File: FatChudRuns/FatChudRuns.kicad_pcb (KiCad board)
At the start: 4 copper layers, 96.9 x 73.9 mm, 104 parts, among them J1 RJ45_Pulse_JXD6-0001NL, J2 Z-21320110021001, J3 FTSH-107-01-L-DV-K-P, J4 TYPE-C-31-M-12, SW1 TS-1187A-B-A-B, SW5 1825360-3, U1 STM32F107RBT6, U2 DP83848I, U3 USBLC6-2SC6, U4 ST730M33R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

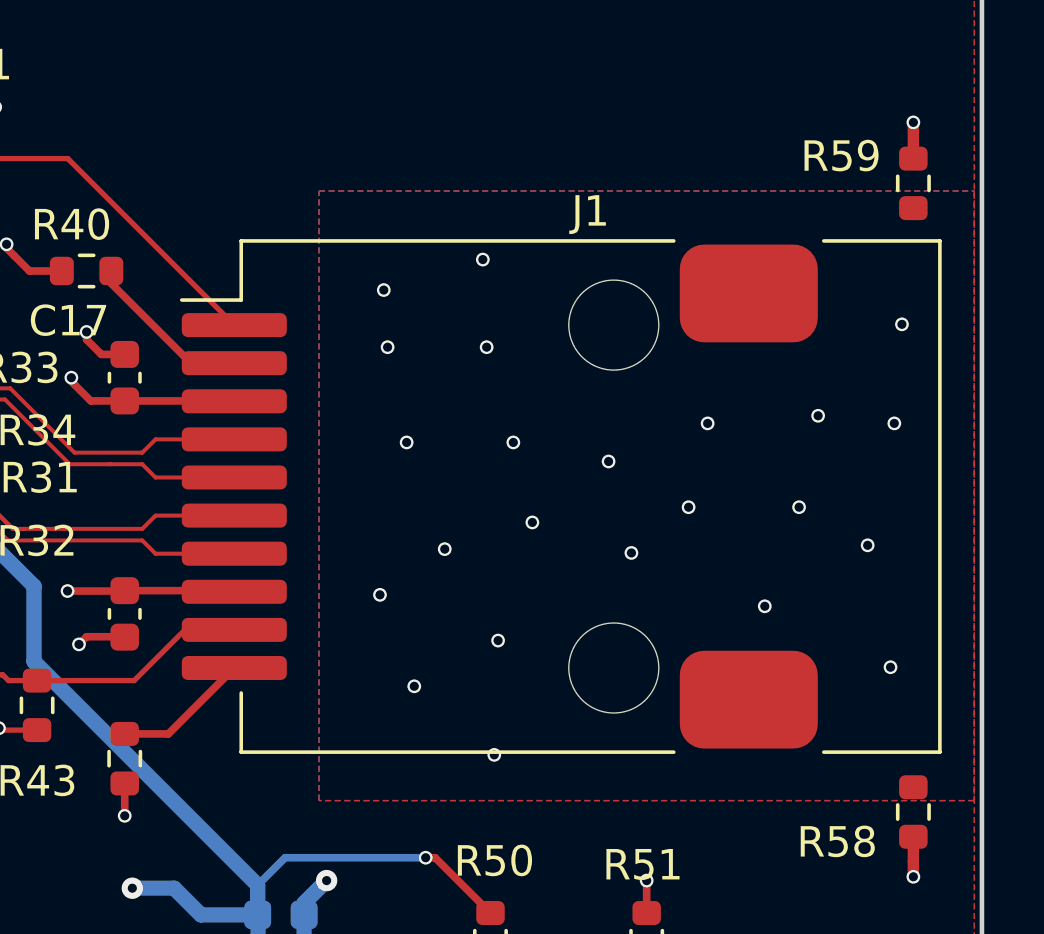
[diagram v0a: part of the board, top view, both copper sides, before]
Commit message: updated 3d model footprint for Rj45 (created new library)
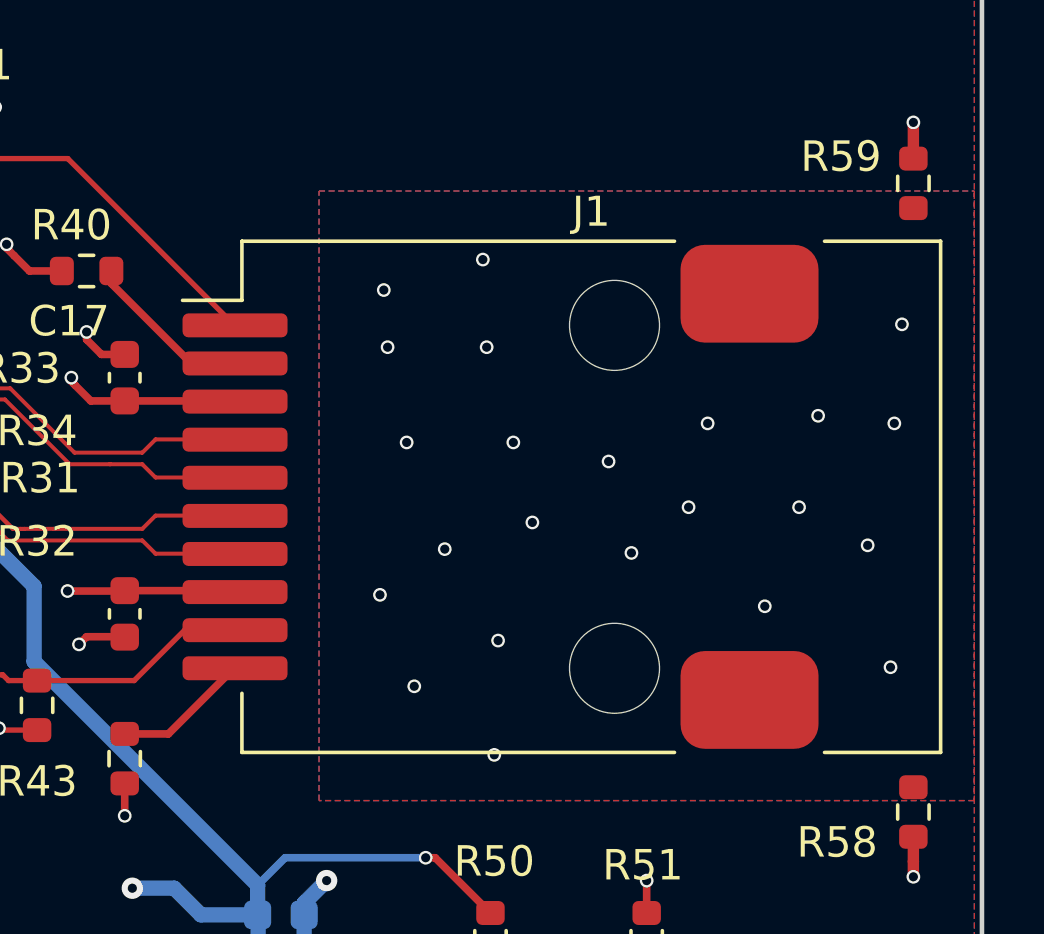
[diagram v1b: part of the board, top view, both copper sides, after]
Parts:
- J1: footprint Connector_RJ:RJ45_Pulse_JXD6-0001NL_Horizontal -> JXD6-0001NL:RJ45_Pulse_JXD6-0001NL_Horizontal

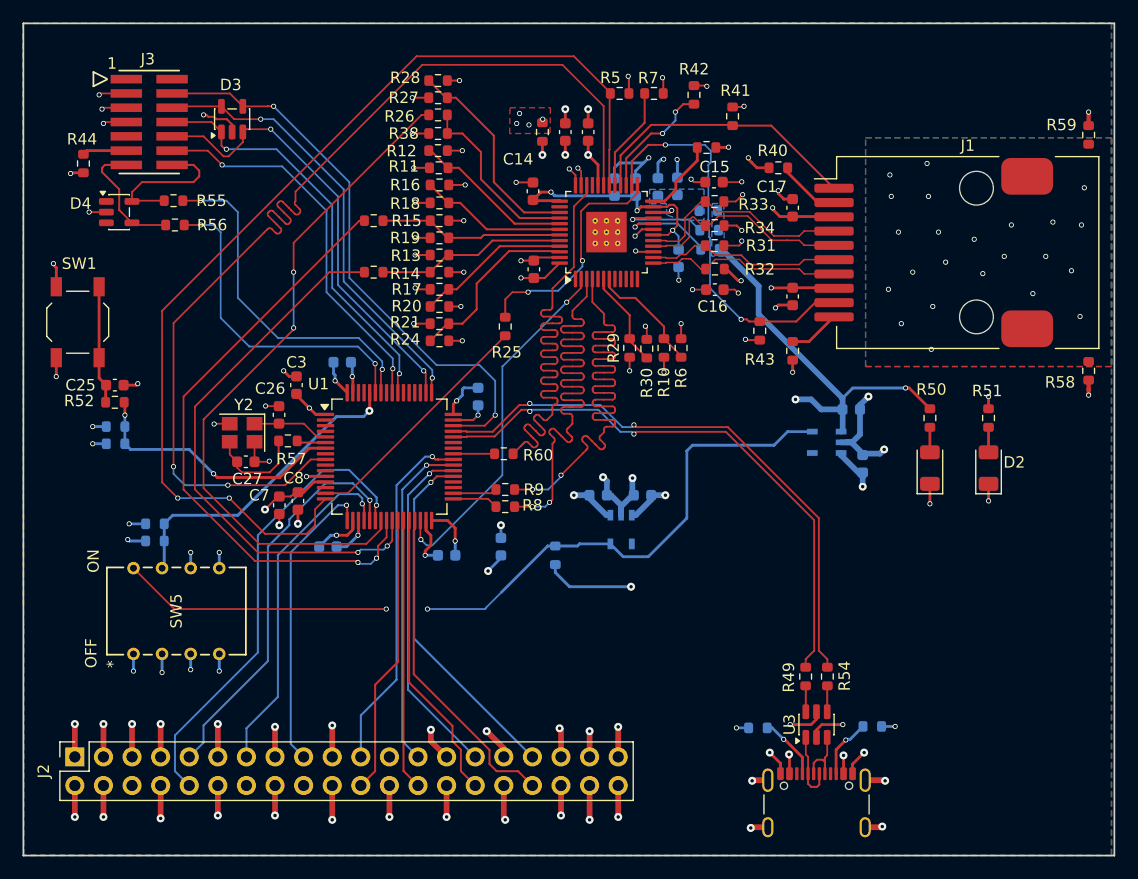
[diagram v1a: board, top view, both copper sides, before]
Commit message: updated 10uF to 0805, completed BOM, sent to fab
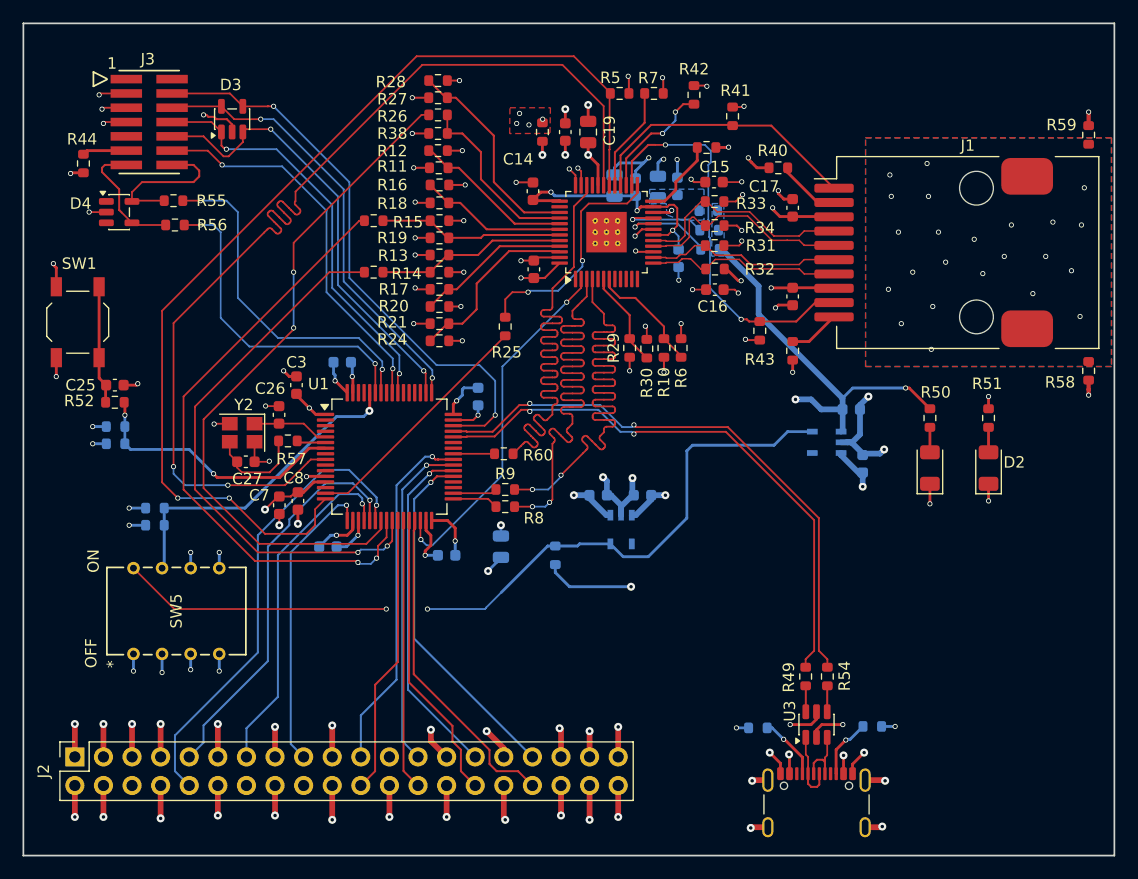
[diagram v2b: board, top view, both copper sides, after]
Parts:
- C1, C11, C19, C9: footprint Capacitor_SMD:C_0603_1608Metric -> Capacitor_SMD:C_0805_2012Metric
- moved R2 1.40 mm to (165.5, 138.6)
- moved R3 1.40 mm to (165.5, 137.0)
- moved C11 0.13 mm to (206.3, 108.4)
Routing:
- net /MCU/BOOT0: track 28.0 -> 28.8 mm
- removed copper zone on B.Cu, net GND
- removed copper zone on F.Cu, net GND
